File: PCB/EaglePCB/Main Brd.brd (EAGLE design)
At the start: 109.2 x 66 mm, 56 parts, among them J1 1909763-1, J3 1909763-1, U1 ATWINC1500-MR210PB1952-T, U3 MSP430FR2355TDBTRDBT0038A_M, U6 ARJM11C7-114-BA-EW2

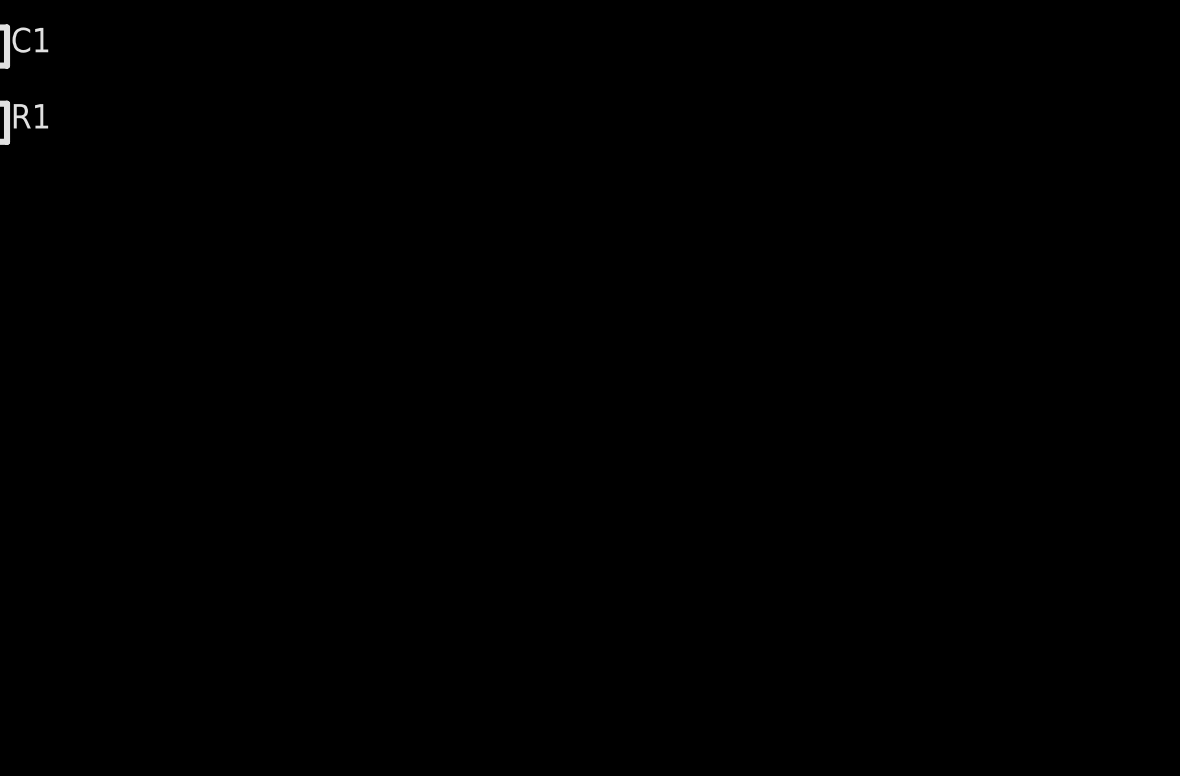
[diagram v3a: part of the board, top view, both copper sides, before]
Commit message: added JTAG Port
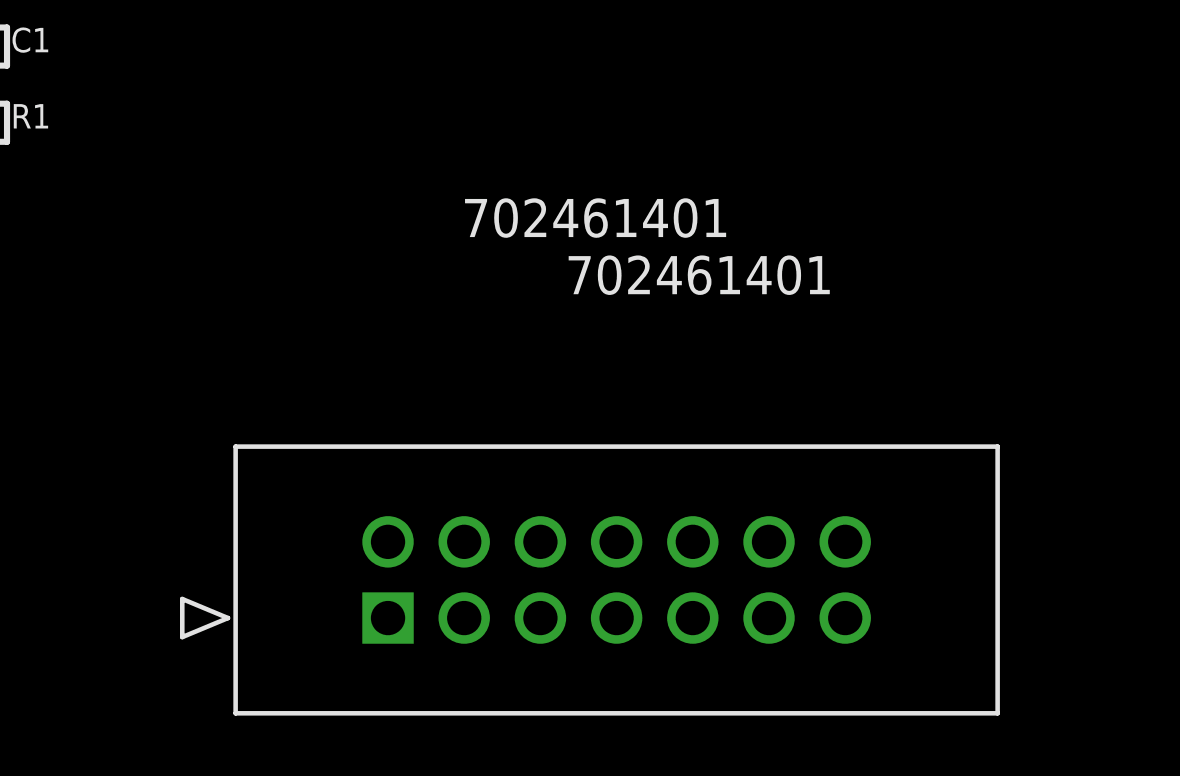
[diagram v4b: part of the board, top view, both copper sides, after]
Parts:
- added J2: 702461401, 473:CON_702461401_MOL
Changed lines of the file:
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@@
 <attribute name="VALUE" x="36.35" y="29.6" size="1.27" layer="28" rot="MR180"/>
+</element>
+<element name="J2" library="473" package="CON_702461401_MOL" value="702461401" x="5.08" y="-53.34" smashed="yes">
+<attribute name="COPYRIGHT" value="Copyright (C) 2022 Ultra Librarian. All rights reserved." x="5.08" y="-53.34" size="1.778" layer="27" display="off"/>
+<attribute name="MANUFACTURER_PART_NUMBER" value="702461401" x="5.08" y="-53.34" size="1.778" layer="27" display="off"/>
+<attribute name="MFR_NAME" value="Molex Connector Corporation" x="5.08" y="-53.34" size="1.778" layer="27" display="off"/>
+<attribute name="NAME" x="9.4234" y="-42.545" size="1.27" layer="27" ratio="6" rot="SR0"/>
+<attribute name="VALUE" x="10.9728" y="-42.545" size="1.27" layer="21" ratio="6" rot="SR0"/>
 </element>
 </elements>

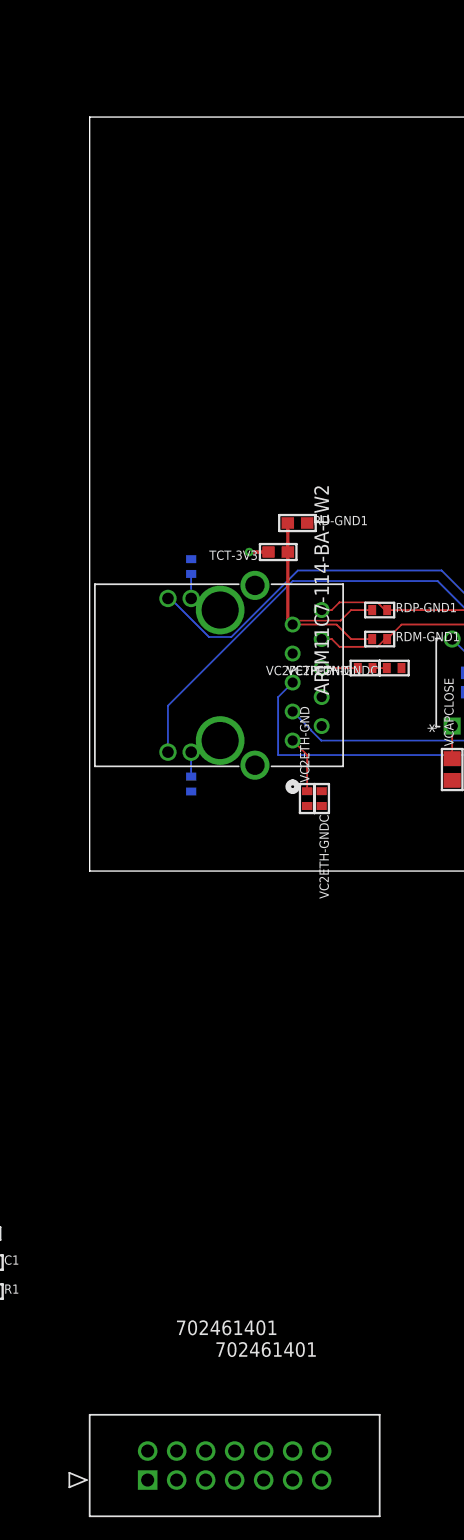
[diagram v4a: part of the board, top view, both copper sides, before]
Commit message: placed JTAG Port
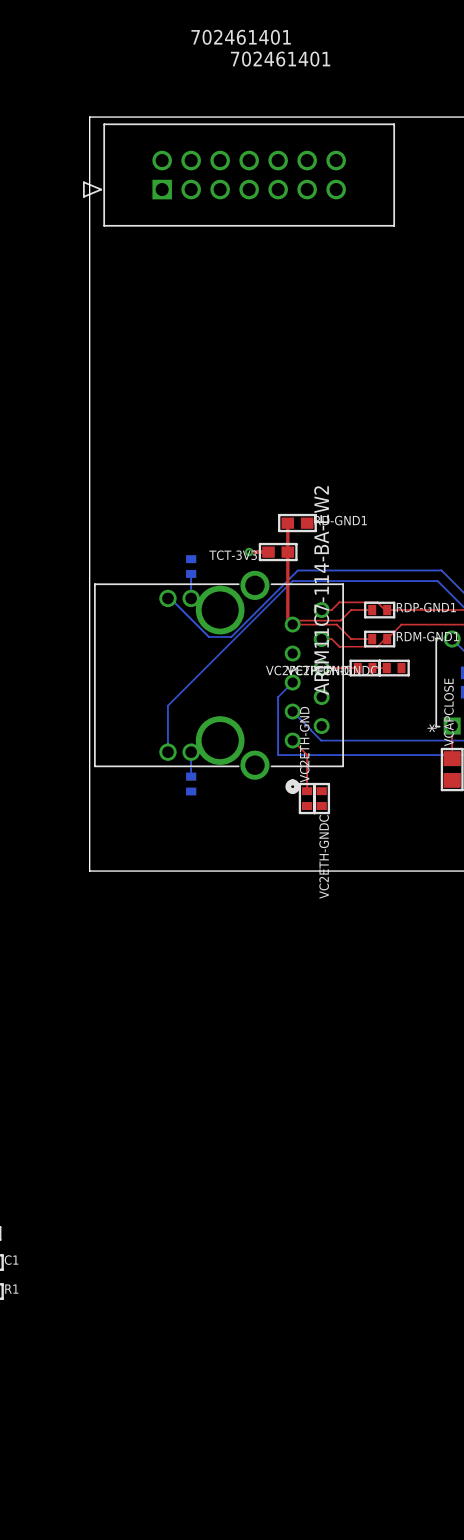
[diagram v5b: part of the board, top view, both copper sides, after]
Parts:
- moved J2 113.0 mm to (6.35, 59.7)
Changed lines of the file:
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@@
 <attribute name="VALUE" x="36.35" y="29.6" size="1.27" layer="28" rot="MR180"/>
 </element>
-<element name="J2" library="473" package="CON_702461401_MOL" value="702461401" x="5.08" y="-53.34" smashed="yes">
-<attribute name="COPYRIGHT" value="Copyright (C) 2022 Ultra Librarian. All rights reserved." x="5.08" y="-53.34" size="1.778" layer="27" display="off"/>
-<attribute name="MANUFACTURER_PART_NUMBER" value="702461401" x="5.08" y="-53.34" size="1.778" layer="27" display="off"/>
-<attribute name="MFR_NAME" value="Molex Connector Corporation" x="5.08" y="-53.34" size="1.778" layer="27" display="off"/>
-<attribute name="NAME" x="9.4234" y="-42.545" size="1.27" layer="27" ratio="6" rot="SR0"/>
-<attribute name="VALUE" x="10.9728" y="-42.545" size="1.27" layer="21" ratio="6" rot="SR0"/>
+<element name="J2" library="473" package="CON_702461401_MOL" value="702461401" x="6.35" y="59.69" smashed="yes">
+<attribute name="COPYRIGHT" value="Copyright (C) 2022 Ultra Librarian. All rights reserved." x="6.35" y="59.69" size="1.778" layer="27" display="off"/>
+<attribute name="MANUFACTURER_PART_NUMBER" value="702461401" x="6.35" y="59.69" size="1.778" layer="27" display="off"/>
+<attribute name="MFR_NAME" value="Molex Connector Corporation" x="6.35" y="59.69" size="1.778" layer="27" display="off"/>
+<attribute name="NAME" x="10.6934" y="70.485" size="1.27" layer="27" ratio="6" rot="SR0"/>
+<attribute name="VALUE" x="12.2428" y="70.485" size="1.27" layer="21" ratio="6" rot="SR0"/>
 </element>
 </elements>

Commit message: added wire labels
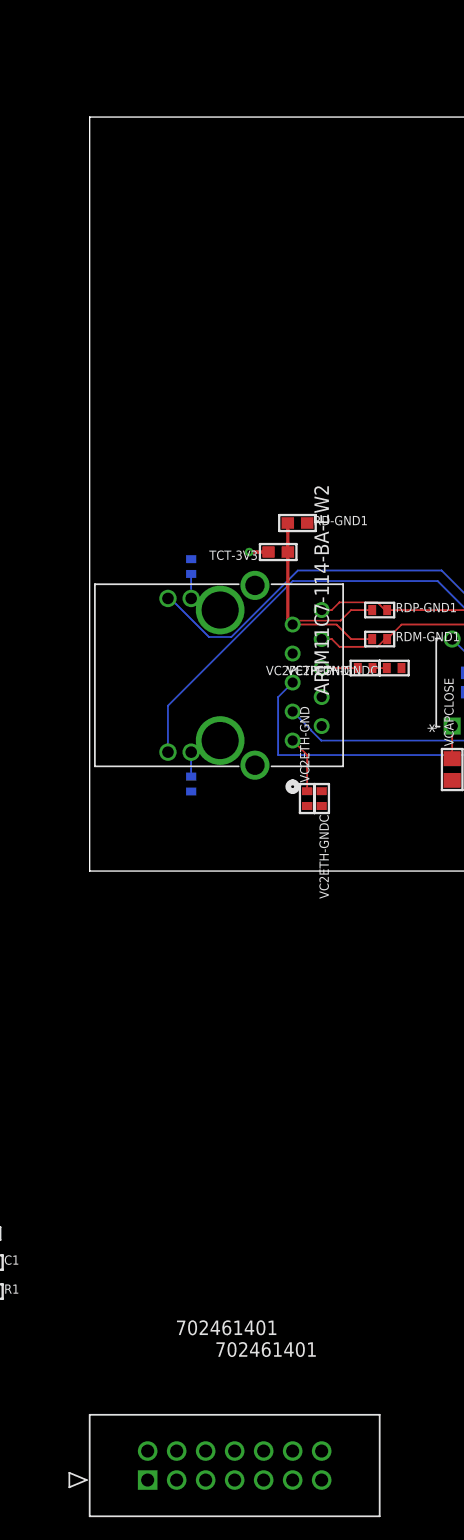
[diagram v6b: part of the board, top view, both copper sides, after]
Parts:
- moved J2 113.0 mm to (5.08, -53.3)
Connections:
- new net ETH_CHIPSEL: ETH.9
- new net ETH_MISO: ETH.6
- new net ETH_MOSI: ETH.7
- new net ETH_SCK: ETH.8
- new net LORA1_CHIPSEL: LORA1.20
- new net LORA1_GPIO_0: LORA1.9
- new net LORA1_MISO: LORA1.19
- new net LORA1_MOSI: LORA1.18
- new net LORA1_SCK: LORA1.17
- new net LORA1_TX: LORA1.23
- new net LORA2_CHIPSEL: LORA2.20
- new net LORA2_GPIO_0: LORA2.9
- new net LORA2_MISO: LORA2.18
- new net LORA2_MOSI: LORA2.19
- new net LORA2_RX: LORA2.23
- new net LORA2_SCK: LORA2.17
- new net N$11: LORA2.6
- new net N$12: LORA2.15
- new net N$13: LORA2.1
- new net N$14: ETH.5
- new net N$15: ETH.3
- net VBAT1: no longer LORA2.1
- net VBAT2: no longer LORA2.15
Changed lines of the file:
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@@
 <layers>
 <layer number="1" name="Top" color="4" fill="1" visible="yes" active="yes"/>
+<layer number="2" name="Route2" color="16" fill="1" visible="no" active="yes"/>
+<layer number="3" name="Route3" color="17" fill="1" visible="no" active="yes"/>
+<layer number="4" name="Route4" color="18" fill="1" visible="no" active="yes"/>
+<layer number="5" name="Route5" color="19" fill="1" visible="no" active="yes"/>
+<layer number="6" name="Route6" color="25" fill="1" visible="no" active="yes"/>
+<layer number="7" name="Route7" color="26" fill="1" visible="no" active="yes"/>
+<layer number="8" name="Route8" color="27" fill="1" visible="no" active="yes"/>
+<layer number="9" name="Route9" color="28" fill="1" visible="no" active="yes"/>
+<layer number="10" name="Route10" color="29" fill="1" visible="no" active="yes"/>
+<layer number="11" name="Route11" color="30" fill="1" visible="no" active="yes"/>
+<layer number="12" name="Route12" color="20" fill="1" visible="no" active="yes"/>
+<layer number="13" name="Route13" color="21" fill="1" visible="no" active="yes"/>
+<layer number="14" name="Route14" color="22" fill="1" visible="no" active="yes"/>
+<layer number="15" name="Route15" color="23" fill="1" visible="no" active="yes"/>
 <layer number="16" name="Bottom" color="1" fill="1" visible="yes" active="yes"/>
 <layer number="17" name="Pads" color="2" fill="1" visible="yes" active="yes"/>
@@
 <attribute name="VALUE" x="36.35" y="29.6" size="1.27" layer="28" rot="MR180"/>
 </element>
-<element name="J2" library="473" package="CON_702461401_MOL" value="702461401" x="6.35" y="59.69" smashed="yes">
-<attribute name="COPYRIGHT" value="Copyright (C) 2022 Ultra Librarian. All rights reserved." x="6.35" y="59.69" size="1.778" layer="27" display="off"/>
-<attribute name="MANUFACTURER_PART_NUMBER" value="702461401" x="6.35" y="59.69" size="1.778" layer="27" display="off"/>
-<attribute name="MFR_NAME" value="Molex Connector Corporation" x="6.35" y="59.69" size="1.778" layer="27" display="off"/>
-<attribute name="NAME" x="10.6934" y="70.485" size="1.27" layer="27" ratio="6" rot="SR0"/>
-<attribute name="VALUE" x="12.2428" y="70.485" size="1.27" layer="21" ratio="6" rot="SR0"/>
+<element name="J2" library="473" package="CON_702461401_MOL" value="702461401" x="5.08" y="-53.34" smashed="yes">
+<attribute name="COPYRIGHT" value="Copyright (C) 2022 Ultra Librarian. All rights reserved." x="5.08" y="-53.34" size="1.778" layer="27" display="off"/>
+<attribute name="MANUFACTURER_PART_NUMBER" value="702461401" x="5.08" y="-53.34" size="1.778" layer="27" display="off"/>
+<attribute name="MFR_NAME" value="Molex Connector Corporation" x="5.08" y="-53.34" size="1.778" layer="27" display="off"/>
+<attribute name="NAME" x="9.4234" y="-42.545" size="1.27" layer="27" ratio="6" rot="SR0"/>
+<attribute name="VALUE" x="10.9728" y="-42.545" size="1.27" layer="21" ratio="6" rot="SR0"/>
 </element>
 </elements>
@@
 </signal>
 <signal name="VBAT1">
-<contactref element="LORA2" pad="1"/>
 <contactref element="LORA1" pad="1"/>
-<wire x1="84.6836" y1="26.08" x2="84.6836" y2="7.03" width="0" layer="19" extent="1-1"/>
 </signal>
 <signal name="VR_ANA">
@@
 </signal>
 <signal name="VBAT2">
-<contactref element="LORA2" pad="15"/>
 <contactref element="LORA1" pad="15"/>
-<wire x1="90.5764" y1="22.18" x2="90.5764" y2="3.13" width="0" layer="19" extent="1-1"/>
 </signal>
 <signal name="GND">
@@
 <wire x1="39.37" y1="25.48" x2="39.37" y2="29.63" width="0.1524" layer="16"/>
 </signal>
+<signal name="N$11">
+<contactref element="LORA2" pad="6"/>
+</signal>
+<signal name="N$12">
+<contactref element="LORA2" pad="15"/>
+</signal>
+<signal name="N$13">
+<contactref element="LORA2" pad="1"/>
+</signal>
+<signal name="LORA2_GPIO_0">
+<contactref element="LORA2" pad="9"/>
+</signal>
+<signal name="LORA2_MOSI">
+<contactref element="LORA2" pad="19"/>
+</signal>
+<signal name="LORA2_MISO">
+<contactref element="LORA2" pad="18"/>
+</signal>
+<signal name="LORA2_SCK">
+<contactref element="LORA2" pad="17"/>
+</signal>
+<signal name="LORA2_CHIPSEL">
+<contactref element="LORA2" pad="20"/>
+</signal>
+<signal name="LORA2_RX">
+<contactref element="LORA2" pad="23"/>
+</signal>
+<signal name="LORA1_TX">
+<contactref element="LORA1" pad="23"/>
+</signal>
+<signal name="LORA1_CHIPSEL">
+<contactref element="LORA1" pad="20"/>
+</signal>
+<signal name="LORA1_MISO">
+<contactref element="LORA1" pad="19"/>
+</signal>
+<signal name="LORA1_MOSI">
+<contactref element="LORA1" pad="18"/>
+</signal>
+<signal name="LORA1_SCK">
+<contactref element="LORA1" pad="17"/>
+</signal>
+<signal name="LORA1_GPIO_0">
+<contactref element="LORA1" pad="9"/>
+</signal>
+<signal name="ETH_CHIPSEL">
+<contactref element="ETH" pad="9"/>
+</signal>
+<signal name="ETH_SCK">
+<contactref element="ETH" pad="8"/>
+</signal>
+<signal name="ETH_MOSI">
+<contactref element="ETH" pad="7"/>
+</signal>
+<signal name="ETH_MISO">
+<contactref element="ETH" pad="6"/>
+</signal>
+<signal name="N$14">
+<contactref element="ETH" pad="5"/>
+</signal>
+<signal name="N$15">
+<contactref element="ETH" pad="3"/>
+</signal>
 </signals>

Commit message: All Passives Complete
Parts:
- added !MSP_RST!_3V3: 47 kOhm, Resistor_Capacitor:RES_0603
- added R2: RC0603JR-070RL, Resistor_Capacitor:RES_0603
- added R3: 10 uF, microbuilder:2012
- added RD-GND2, RD-GND3, RD-GND4: 0.1 uF, microbuilder:0603
- added TCXO1, TCXO2: TCXO_32,000MHZ, 473:TCXO
- moved J2 112.9 mm to (38.1, 54.6), turned to 180 degrees
- moved U1 5.08 mm to (95.2, 52.1)
- moved U3 1.27 mm to (52.1, 53.3), turned to 90 degrees
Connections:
- net ETH_CHIPSEL renamed !ETH_CHIPSEL
- net LORA1_GPIO_0 renamed LORA1_IRQ
- net LORA2_GPIO_0 renamed LORA2_IRQ
- net N$11 renamed LORA2_RST
- net N$3 renamed NC_1
- net RDM renamed RD_N
- net RDP renamed RD_P
- net TDC renamed TD_C
- net TDM renamed TD_N
- net TDP renamed TD_P
- removed net DVCC: U3.10
- removed net DVSS: U3.11
- removed net VBAT1: LORA1.1
- removed net VBAT2: LORA1.15
- removed net VDDIO: U1.23
- removed net VDDOSC_ETH: ETH.25, VSSOSC-VDDOSC.1
- removed net VDDPLL_ETH: ETH.20, VSSPLL-VDDPLL.1
- removed net VDDRX_ETH: ETH.19, VSSRX-VDDRX.2
- removed net VDDTX_ETH: ETH.15, VSSTX-VDDTX.2
- removed net VDD_ETH: ETH.28, VSS-VDD_ETH.2
- removed net VSSOSC_ETH: ETH.22, VSSOSC-VDDOSC.2
- removed net VSSPLL_ETH: ETH.21, VSSPLL-VDDPLL.2
- removed net VSSRX_ETH: ETH.11, VSSRX-VDDRX.1
- removed net VSSTX_ETH: ETH.18, VSSTX-VDDTX.1
- removed net VSS_ETH: ETH.2, VSS-VDD_ETH.1
- new net !ATC_IRQ: U1.13
- new net !ATC_RST: U1.4
- new net !ETH_IRQ: ETH.4
- new net !ETH_RST: ETH.10
- new net !MSP_RST: !MSP_RST!_3V3.1, J2.11, U3.9
- new net A0_CLK: J2.5, U3.30
- new net A0_MISO: J2.3, U3.29
- new net A0_MOSI: J2.1, U3.28
- new net A1_CLK: U3.22
- new net A1_MISO: U3.21
- new net A1_MOSI: U3.20
- new net ATC_EN: U1.22
- new net ATC_MISO: U1.17
- new net ATC_MOSI: U1.15
- new net ATC_SPI_CFG: R2.2, U1.10
- new net ATC_SSN: U1.16
- new net B0_CLK: U3.6
- new net B0_MISO: U3.5
- new net B0_MOSI: U3.4
- new net B1_CLK: U3.18
- new net B1_MISO: U3.17
- new net B1_MOSI: U3.16
- new net LORA1_RST: LORA1.6
- new net MSP_TCK: J2.7, U3.31
- new net MSP_TEST: J2.8, U3.8
- new net MSP_VCC: J2.2
- new net MSP_VCC_TAR: J2.4
- new net N$21: U3.23
- new net N$3: LORA1.21
- new net SPI_SCK: U1.18
- new net XTA1: LORA1.4, TCXO1.OSC
- new net XTA2: LORA2.4, TCXO2.OSC
- net 3V3: now also !MSP_RST!_3V3.2, ETH.15, ETH.19, ETH.20, ETH.25, ETH.28, LORA1.1, LORA1.15, LORA2.1, LORA2.15, R2.1, RD-GND2.1, RD-GND3.1, TCXO1.VCC, TCXO2.VCC, U1.23, U3.10, VSS-VDD_ETH.2, VSSOSC-VDDOSC.1, VSSPLL-VDDPLL.1, VSSRX-VDDRX.2, VSSTX-VDDTX.2
- net GND: now also ETH.11, ETH.18, ETH.2, ETH.21, ETH.22, J2.9, LORA1.7, LORA1.8, LORA2.7, LORA2.8, R3.2, RD-GND2.2, RD-GND3.2, RD-GND4.1, TCXO1.GND, TCXO2.GND, U1.12, U1.28, U1.29, U1.9, U3.11, VSS-VDD_ETH.1, VSSOSC-VDDOSC.2, VSSPLL-VDDPLL.2, VSSRX-VDDRX.1, VSSTX-VDDTX.1
- net N$12: now also LORA2.21; no longer LORA2.15
- net N$13: now also R3.1, RD-GND4.2, U1.24; no longer LORA2.1
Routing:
- net GND: track 0.00 -> 73.9 mm, vias 0 -> 16
- net 3V3: track 1.69 -> 31.7 mm
- net RD_N: track 45.4 -> 54.5 mm
- net N$8: track 4.00 -> 11.0 mm
- net VSSTX_ETH: track 5.04 -> 0.00 mm
- net VDDTX_ETH: track 5.04 -> 0.00 mm
- net VSSOSC_ETH: track 4.01 -> 0.00 mm
- net VDDOSC_ETH: track 4.01 -> 0.00 mm
- net XTA1: track 0.00 -> 3.77 mm
- net XTA2: track 0.00 -> 3.77 mm
- net VDD_ETH: track 3.49 -> 0.00 mm
- net VDDRX_ETH: track 3.49 -> 0.00 mm
- net VSS_ETH: track 3.49 -> 0.00 mm
- net VSSRX_ETH: track 3.49 -> 0.00 mm
- net TD_P: track 41.0 -> 44.0 mm
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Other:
- board size 109.2 x 66 mm -> 110.5 x 90.2 mm
